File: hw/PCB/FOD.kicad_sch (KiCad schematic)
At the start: 8 parts, among them J2 Comm_port, U1 SAMD21G, Y1 32.768kHz

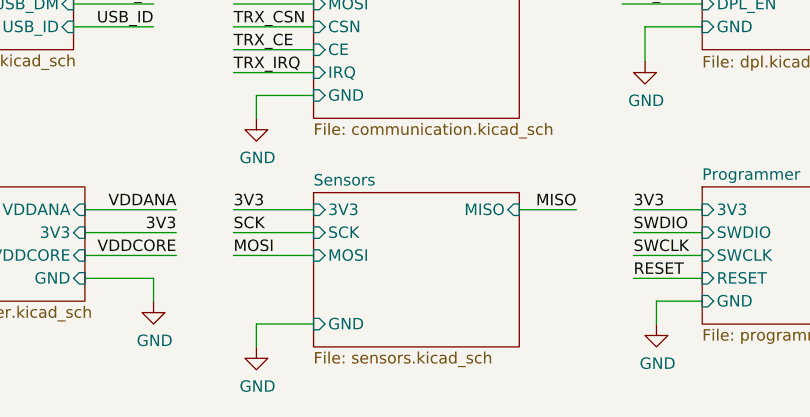
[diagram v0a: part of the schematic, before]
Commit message: Deleted old files and added a BOM.
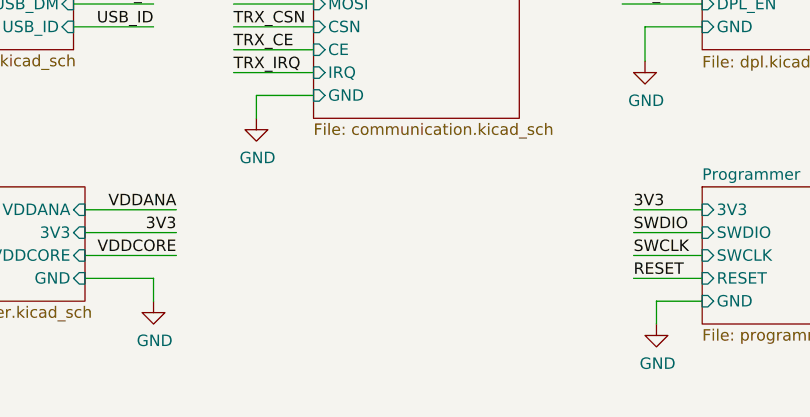
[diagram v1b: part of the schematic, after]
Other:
- removed sheet Sensors
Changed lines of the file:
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@@
 (kicad_sch (version 20200512) (host eeschema "5.99.0-unknown-57e35c9~88~ubuntu19.10.1")
-  (page 1 7)
+  (page 1 6)
   (paper "A4")
   (junction (at 88.9 45.72))
   (junction (at 95.25 58.42))
   (junction (at 101.6 45.72))
-  (no_connect (at 120.65 90.17))
+  (no_connect (at 120.65 59.69))
+  (no_connect (at 163.83 64.77))
+  (no_connect (at 120.65 52.07))
   (no_connect (at 163.83 36.83))
+  (no_connect (at 163.83 82.55))
+  (no_connect (at 163.83 87.63))
+  (no_connect (at 163.83 95.25))
+  (no_connect (at 120.65 54.61))
+  (no_connect (at 120.65 41.91))
+  (no_connect (at 163.83 39.37))
+  (no_connect (at 163.83 85.09))
   (no_connect (at 163.83 62.23))
-  (no_connect (at 120.65 41.91))
-  (no_connect (at 120.65 52.07))
-  (no_connect (at 163.83 85.09))
-  (no_connect (at 163.83 39.37))
-  (no_connect (at 120.65 54.61))
-  (no_connect (at 163.83 82.55))
-  (no_connect (at 163.83 95.25))
-  (no_connect (at 163.83 64.77))
-  (no_connect (at 120.65 59.69))
+  (no_connect (at 163.83 59.69))
   (no_connect (at 120.65 44.45))
   (no_connect (at 163.83 90.17))
-  (no_connect (at 163.83 59.69))
-  (no_connect (at 163.83 87.63))
   (no_connect (at 120.65 57.15))
+  (no_connect (at 120.65 90.17))
   (wire (pts (xy 76.2 78.105) (xy 83.185 78.105))
     (stroke (width 0) (type solid) (color 0 0 0 0))
@@
     (stroke (width 0) (type solid) (color 0 0 0 0))
   )
-  (wire (pts (xy 116.84 139.7) (xy 125.73 139.7))
-    (stroke (width 0) (type solid) (color 0 0 0 0))
-  )
-  (wire (pts (xy 116.84 142.24) (xy 125.73 142.24))
-    (stroke (width 0) (type solid) (color 0 0 0 0))
-  )
-  (wire (pts (xy 116.84 144.78) (xy 125.73 144.78))
-    (stroke (width 0) (type solid) (color 0 0 0 0))
-  )
   (wire (pts (xy 119.38 127) (xy 119.38 129.54))
     (stroke (width 0) (type solid) (color 0 0 0 0))
   )
-  (wire (pts (xy 119.38 152.4) (xy 119.38 154.94))
-    (stroke (width 0) (type solid) (color 0 0 0 0))
-  )
-  (wire (pts (xy 119.38 152.4) (xy 125.73 152.4))
-    (stroke (width 0) (type solid) (color 0 0 0 0))
-  )
   (wire (pts (xy 125.73 114.3) (xy 116.84 114.3))
     (stroke (width 0) (type solid) (color 0 0 0 0))
@@
     (stroke (width 0) (type solid) (color 0 0 0 0))
   )
-  (wire (pts (xy 148.59 139.7) (xy 154.94 139.7))
-    (stroke (width 0) (type solid) (color 0 0 0 0))
-  )
   (wire (pts (xy 160.02 111.76) (xy 168.91 111.76))
     (stroke (width 0) (type solid) (color 0 0 0 0))
@@
     (effects (font (size 1.27 1.27)) (justify left bottom))
   )
-  (label "3V3" (at 116.84 139.7 0)
-    (effects (font (size 1.27 1.27)) (justify left bottom))
-  )
-  (label "SCK" (at 116.84 142.24 0)
-    (effects (font (size 1.27 1.27)) (justify left bottom))
-  )
-  (label "MOSI" (at 116.84 144.78 0)
-    (effects (font (size 1.27 1.27)) (justify left bottom))
-  )
   (label "MISO" (at 154.94 111.76 180)
-    (effects (font (size 1.27 1.27)) (justify right bottom))
-  )
-  (label "MISO" (at 154.94 139.7 180)
     (effects (font (size 1.27 1.27)) (justify right bottom))
   )
@@
     )
     (property "Datasheet" "" (id 3) (at 119.38 129.54 0)
-      (effects (font (size 1.27 1.27)) hide)
-    )
-  )
-  (symbol (lib_id "power:GND") (at 119.38 154.94 0) (unit 1)
-    (property "Reference" "#PWR01" (id 0) (at 119.38 161.29 0)
-      (effects (font (size 1.27 1.27)) hide)
-    )
-    (property "Value" "GND" (id 1) (at 119.507 159.3342 0))
-    (property "Footprint" "" (id 2) (at 119.38 154.94 0)
-      (effects (font (size 1.27 1.27)) hide)
-    )
-    (property "Datasheet" "" (id 3) (at 119.38 154.94 0)
       (effects (font (size 1.27 1.27)) hide)
     )
@@
     )
   )
-  (sheet (at 125.73 137.795) (size 22.86 17.145)
-    (stroke (width 0.001) (type solid) (color 132 0 132 1))
-    (fill (color 255 255 255 0.0000))
-    (property "Sheet name" "Sensors" (id 0) (at 125.73 137.1591 0)
-      (effects (font (size 1.27 1.27)) (justify left bottom))
-    )
-    (property "Sheet file" "sensors.kicad_sch" (id 1) (at 125.73 155.4489 0)
-      (effects (font (size 1.27 1.27)) (justify left top))
-    )
-    (pin "SCK" input (at 125.73 142.24 180)
-      (effects (font (size 1.27 1.27)) (justify left))
-    )
-    (pin "MISO" input (at 148.59 139.7 0)
-      (effects (font (size 1.27 1.27)) (justify right))
-    )
-    (pin "MOSI" input (at 125.73 144.78 180)
-      (effects (font (size 1.27 1.27)) (justify left))
-    )
-    (pin "GND" input (at 125.73 152.4 180)
-      (effects (font (size 1.27 1.27)) (justify left))
-    )
-    (pin "3V3" input (at 125.73 139.7 180)
-      (effects (font (size 1.27 1.27)) (justify left))
-    )
-  )
   (sheet (at 82.55 109.22) (size 16.51 12.7)
     (stroke (width 0) (type solid) (color 132 0 132 1))
@@
   )
   (symbol_instances
-    (path "/53a3f332-f879-40dc-ba4c-3d1c6b16f2f1"
-      (reference "#PWR01") (unit 1)
-    )
     (path "/00000000-0000-0000-0000-00005b67c424"
       (reference "#PWR0101") (unit 1)
